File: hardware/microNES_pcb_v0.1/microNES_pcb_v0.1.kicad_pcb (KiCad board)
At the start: 4 copper layers, 72.3 x 70 mm, 104 parts, among them J1 USB_C_Receptacle_USB2.0_16P, J3 HDMI_E, J4 SM03B-SRSS-TB, J5 Conn_01x05, Q1 2N7002, SW3 PTS810SJM250SMTRLFS, SW4 PTS810SJM250SMTRLFS, U1 RP2350_60QFN, U2 AMS1117-3.3, U3 W25Q128JVS, U5 AMS1117-3.3, Y1 ABM8-272-T3

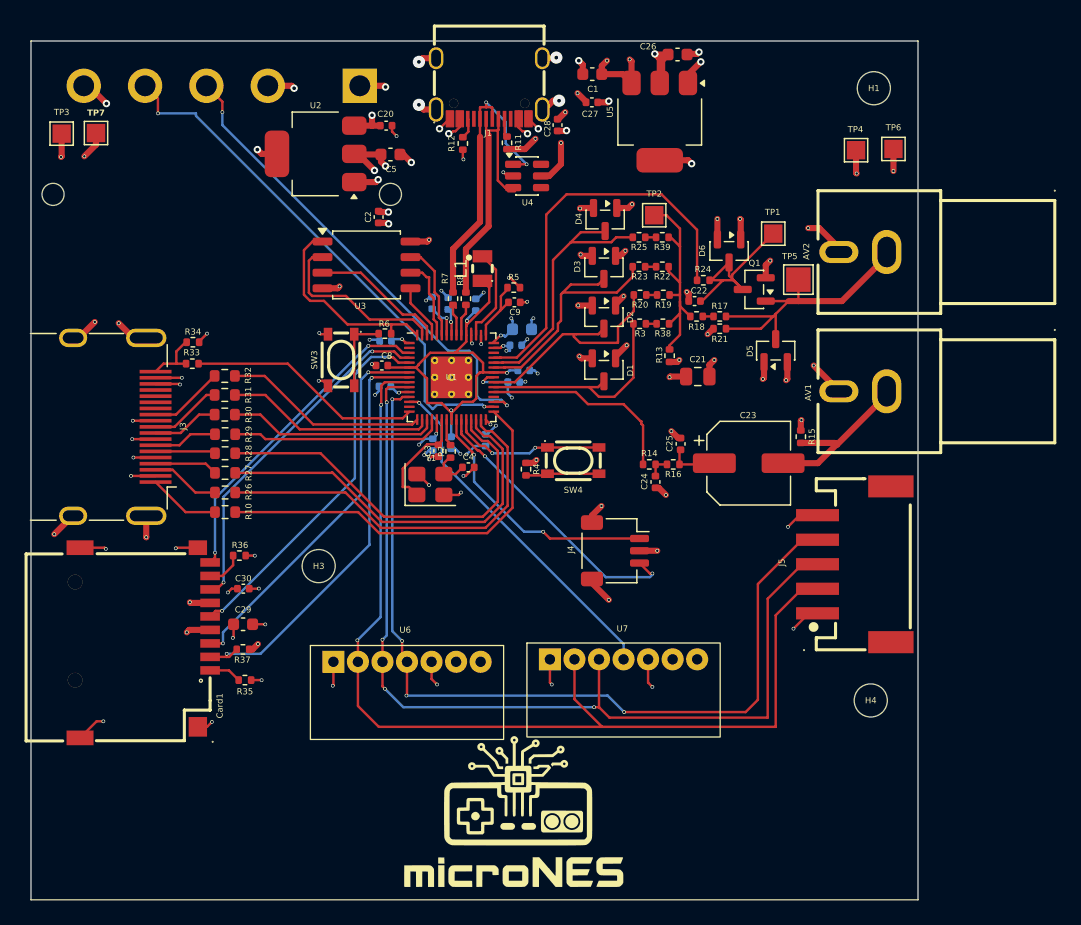
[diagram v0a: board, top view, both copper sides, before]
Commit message: MicroNES full PCB! Wire up the v0.1 PCB peripherals (#29)
* Pico: derive peripheral pin assignments from PCB v0.1 schematic

Add a canonical board pinout header sourced from
hardware/microNES_pcb_v0.1/microNES_pcb_v0.1.kicad_sch, and a
MICRONES_BOARD CMake option (breadboard|v0_1) that drives it into
every Pico pin header.  Default behaviour is unchanged.

With -DMICRONES_BOARD=v0_1 the firmware now uses the silkscreen
nets: video DAC on GP24-27 (GP_VDAC_SUM0..3) with sync clamp on
GP28 (GP_VDAC_GATE); audio PWM on GP23 (GP_ADAC_IN); NES
controller on GP6/7/8 (NES_CLOCK/LATCH/DATA_1); SD card on
GP1-5 (unchanged, already matched the PCB).

* Pico: read both NES controllers from the v0.1 PCB

The v0.1 PCB routes a second 4021 controller port: CLOCK and LATCH are
shared with player 1 on GP6/GP7, and a second DATA line comes back on
GP9 (NES_DATA_2).  Reading both ports therefore costs the same eight
clock edges as reading one — only the GPIO sample inside the shift
loop changes.

Extend the platform driver with nes_hw_controller_read_pair() that
samples both DATA lines per shift step, and surface it through
pico_input_read_pair() returning a {p1, p2} struct.  main.c reads the
pair each frame: player 1 still drives the AppShell (menu nav and
exit combo), player 2 is routed straight to NES controller port 2
($4017).  On boards without PICO_NES_CTL_DATA_P2 (breadboard
default) the second port is reported as "no buttons", so existing
single-port behaviour is preserved.

The NES core already exposed controllers[2], so no emulator changes
were required.  The ESP32-S3 reference driver gains a one-port
wrapper for source-compatibility.

* Pico: drive PWR_LED and read RST_BTN on the v0.1 PCB

Add a small pico_status module that brings up the v0.1 front-panel I/O:

* GP21 (PWR_LED) — configured as output and driven to the lit state in
  pico_status_init(), so the panel LED comes on as soon as the firmware
  reaches the bring-up phase.  Defaults to active-HIGH (common-anode
  pa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
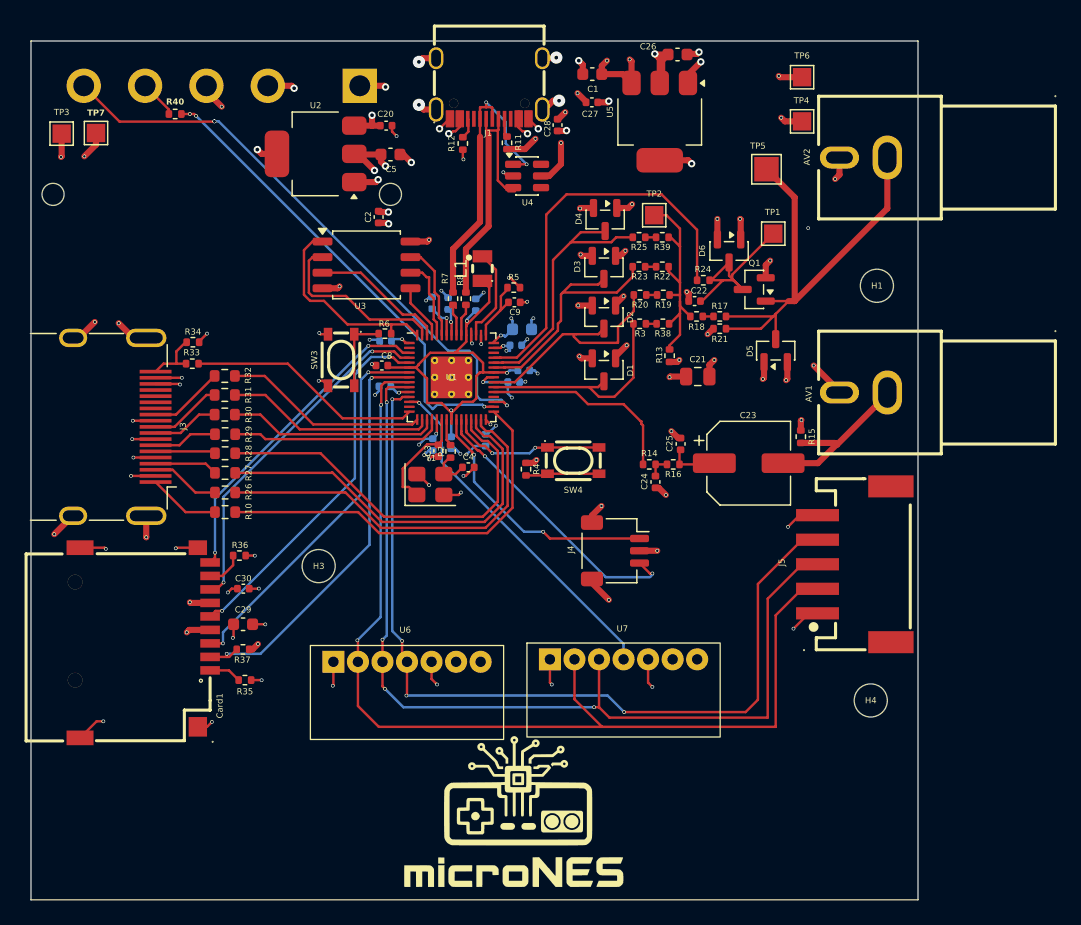
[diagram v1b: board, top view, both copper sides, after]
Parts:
- added R40: 330, Resistor_SMD:R_0402_1005Metric, F.Cu at (100.9, 71.6)
- C19, C29: value 10u -> 10uF
- moved H1 16.1 mm to (158.1, 85.6)
- moved TP6 9.47 mm to (152.0, 68.6)
- moved TP5 9.37 mm to (149.1, 76.1)
- moved AV2 7.70 mm to (157.0, 75.2)
- moved TP4 4.99 mm to (152.0, 72.2)
- moved AV1 0.11 mm to (157.0, 94.3)
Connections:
- U8 pad 3: /PWR_LED -> +3V3
- U8 pad 4: /RST_BTN -> Net-(U8-RST_OUT)
- U8 pad 5: +3V3 -> /PWR_LED
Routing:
- net /VDAC_OUT: track 25.4 -> 40.8 mm
- net /PWR_LED: track 39.5 -> 48.8 mm, vias 2 -> 3
- net /RST_BTN: track 43.9 -> 38.3 mm, vias 2 -> 3
- net Net-(U8-RST_OUT): track 0.00 -> 3.90 mm
- net GND: track 115.2 -> 113.5 mm, vias 81 -> 82
